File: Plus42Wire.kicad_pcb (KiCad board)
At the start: 2 copper layers, 60.8 x 99.9 mm, 32 parts, among them CN1 EDGE_CONN, CN2 CONN_I2C_1, CN3 CONN_I2C_1, CN4 CONN_I2C_1, U1 GAL20V8, U2 PCF8584, U3 24LC16, U4 DS1307+, Y1 12 MHz, Y2 32768 kHz

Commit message: Add 3.3V bus
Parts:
- removed R7: 47, Resistor_THT:R_Axial_DIN0207_L6.3mm_D2.5mm_P2.54mm_Vertical
- added C10: 10u, Capacitor_THT:CP_Radial_D6.3mm_P2.50mm, F.Cu at (135.3, 87.5)
- added C8: 100n, Capacitor_THT:C_Disc_D7.0mm_W2.5mm_P5.00mm, F.Cu at (125.1, 79.9)
- added C9: 100n, Capacitor_THT:C_Disc_D7.0mm_W2.5mm_P5.00mm, F.Cu at (135.3, 74.9)
- added CN5: CONN_I2C_3V3, Connector_PinHeader_2.54mm:PinHeader_1x04_P2.54mm_Vertical, F.Cu at (126.4, 68.5)
- added CN6: CONN_I2C_3V3, Connector_PinHeader_2.54mm:PinHeader_1x04_P2.54mm_Vertical, F.Cu at (148.3, 68.5)
- added CN7: CONN_I2C_3V3, Connector_PinHeader_2.54mm:PinHeader_1x04_P2.54mm_Vertical, F.Cu at (170.4, 68.5)
- added Q1: TN2106, Package_TO_SOT_THT:TO-92L_HandSolder, F.Cu at (139.6, 79.9)
- added Q2: TN2106, Package_TO_SOT_THT:TO-92L_HandSolder, F.Cu at (140.3, 76.2)
- added R4: 47, Resistor_THT:R_Axial_DIN0207_L6.3mm_D2.5mm_P10.16mm_Horizontal, F.Cu at (125.1, 92.6)
- added R5: 4.7k, Resistor_THT:R_Axial_DIN0207_L6.3mm_D2.5mm_P10.16mm_Horizontal, F.Cu at (148.7, 83.1)
- added R6: 4.7k, Resistor_THT:R_Axial_DIN0207_L6.3mm_D2.5mm_P10.16mm_Horizontal, F.Cu at (144.9, 83.1)
- added U5: MCP1700-3302E_TO92, Package_TO_SOT_THT:TO-92L_HandSolder, F.Cu at (130.2, 78.9)
- CN2: renamed from CN4; value CONN_I2C_1 -> CONN_I2C_5V
- CN3: renamed from CN2; value CONN_I2C_1 -> CONN_I2C_5V
- CN4: renamed from CN3; value CONN_I2C_1 -> CONN_I2C_5V
- moved Y2 14.2 mm to (141.1, 102.2)
- moved CN4 10.6 mm to (170.3, 52.8), turned to 90 degrees
- moved FB2 9.25 mm to (125.1, 87.5), turned to 0 degrees
- moved CN3 8.82 mm to (148.3, 52.8), turned to 90 degrees
- moved CN2 8.13 mm to (126.4, 52.8), turned to 90 degrees
- moved C3 6.39 mm to (144.9, 90.8), turned to 0 degrees
- moved BAT1 0.37 mm to (172.5, 81.2)
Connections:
- Y2 pad 1: Net-(U4-Pad2) -> Net-(U4-Pad1)
- Y2 pad 2: Net-(U4-Pad1) -> Net-(U4-Pad2)
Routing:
- net +3V3: track 0.00 -> 97.9 mm
- net /scl_3v3: track 0.00 -> 72.1 mm, vias 0 -> 1
- net /sda_3v3: track 0.00 -> 62.6 mm, vias 0 -> 1
- net +5V: track 243.0 -> 288.0 mm, vias 2 -> 3
- net /scl: track 161.1 -> 179.5 mm, vias 2 -> 3
- net /sda: track 168.7 -> 184.7 mm, vias 4 -> 5
- net Net-(U4-Pad1): track 13.8 -> 3.81 mm
- net Net-(FB2-Pad2): track 3.62 -> 8.26 mm
- net Net-(U4-Pad2): track 13.8 -> 10.4 mm
- net /clock: track 42.3 -> 45.5 mm
- net Net-(R4-Pad1): track 13.1 -> 13.6 mm
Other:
- board text added: "+3.3V"
- board text added: "+5V"
- board text added: "GND"
- board text added: "SCL"
- board text added: "SDA"

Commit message: Ready for V1rc1
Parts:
- C10: footprint Capacitor_THT:CP_Radial_D6.3mm_P2.50mm -> Capacitor_THT:CP_Radial_D5.0mm_P2.00mm
- CN4: value CONN_I2C_5V -> CONN_I2C_5V_ALT
- CN7: value CONN_I2C_3V3 -> CONN_I2C_3V3_ALT
- V1: footprint SoundX:logo -> Plus42Wire:Logo
- moved V1 1.82 mm to (146.1, 135.6)
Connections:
- CN4 pad 1: GND -> +5V
- CN4 pad 2: +5V -> GND
- CN4 pad 3: /sda -> /scl
- CN4 pad 4: /scl -> /sda
- CN7 pad 1: GND -> +3V3
- CN7 pad 2: +3V3 -> GND
- CN7 pad 3: /sda_3v3 -> /scl_3v3
- CN7 pad 4: /scl_3v3 -> /sda_3v3
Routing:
- net /scl: track 179.5 -> 175.1 mm
- net /scl_3v3: track 72.1 -> 67.7 mm
- net /sda: track 184.7 -> 187.2 mm
- net +3V3: track 97.9 -> 95.3 mm
- net /sda_3v3: track 62.6 -> 65.1 mm
- net Net-(BAT1-Pad1): track 23.5 -> 24.9 mm
- net +5V: track 288.0 -> 286.7 mm, vias 3 -> 2
- net /d1: track 31.0 -> 32.1 mm
- net /~rd8584: track 27.5 -> 28.0 mm
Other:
- board text added: "12 MHz"
- board text added: "3.3V BUS"
- board text added: "5V BUS"
- board text added: "CR2032"
- board text added: "DIFFERENT"
- board text added: "PINOUT"

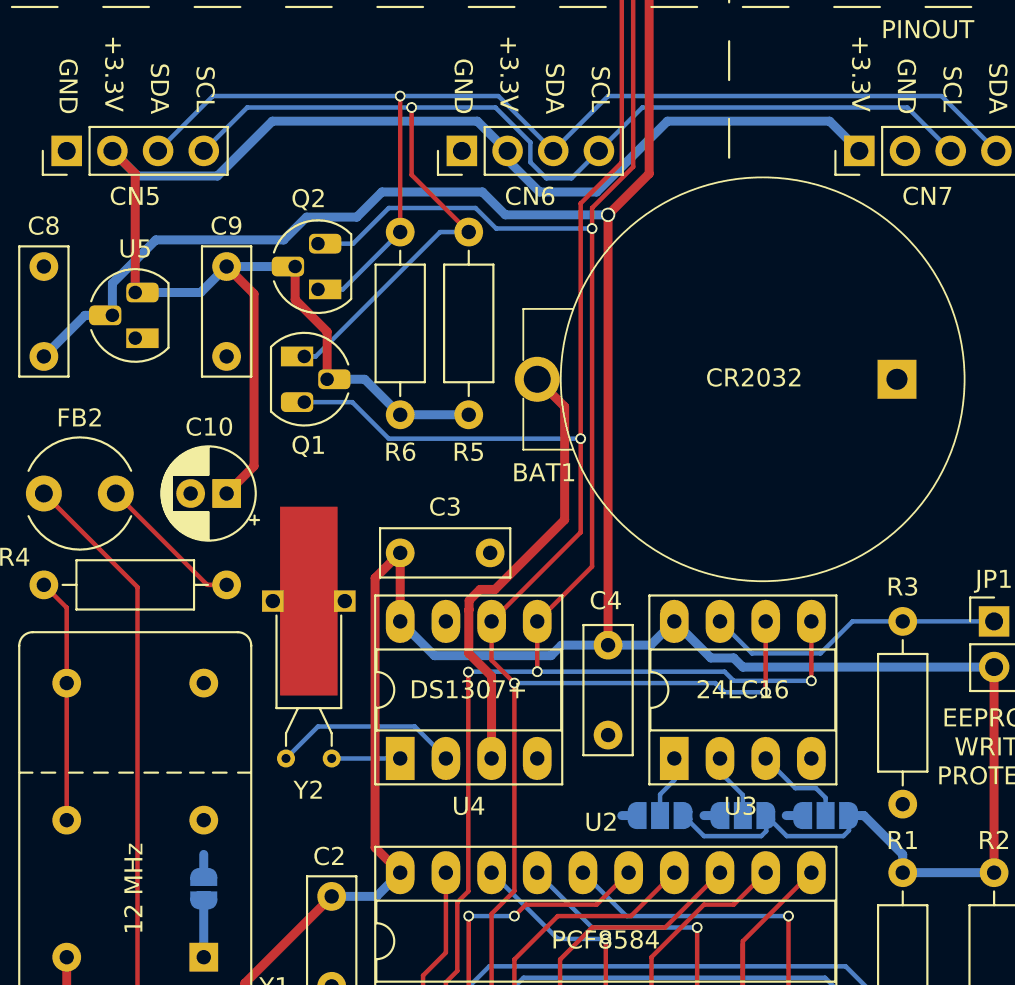
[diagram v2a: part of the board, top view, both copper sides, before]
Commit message: Add footprints for alternative MOSFETs
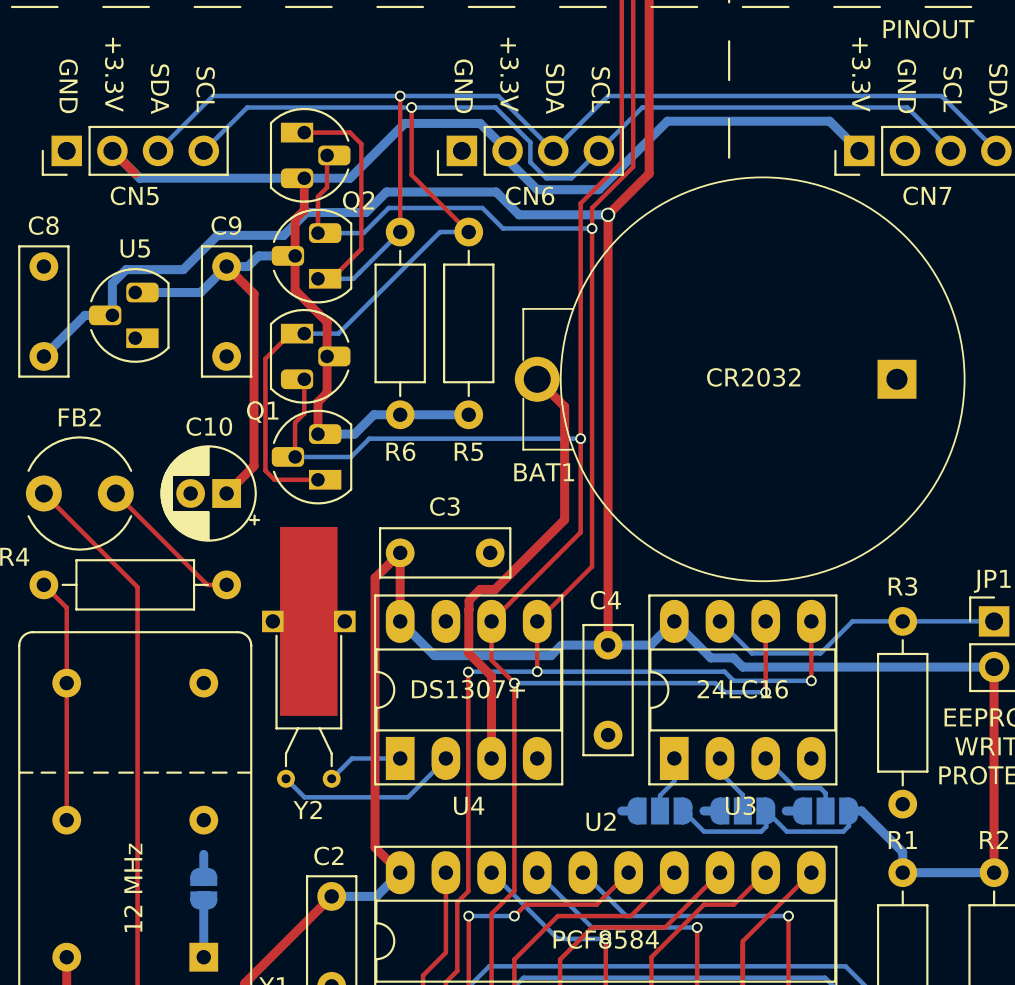
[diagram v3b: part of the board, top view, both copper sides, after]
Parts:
- added Q101: BSS88, Package_TO_SOT_THT:TO-92L_HandSolder, F.Cu at (140.3, 86.7)
- added Q102: BSS88, Package_TO_SOT_THT:TO-92L_HandSolder, F.Cu at (139.6, 67.4)
- moved Q1 1.27 mm to (139.6, 78.6)
- moved Y2 1.13 mm to (141.1, 103.4)
- moved Q2 0.59 mm to (140.3, 75.6)
- moved JP3 0.25 mm to (159.4, 105.2)
- moved JP4 0.25 mm to (164.0, 105.2)
- moved JP5 0.25 mm to (168.6, 105.2)
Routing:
- net /sda_3v3: track 65.1 -> 77.2 mm
- net /scl_3v3: track 67.7 -> 79.3 mm
- net /scl: track 175.1 -> 179.7 mm
- net /sda: track 187.2 -> 191.5 mm
- net +3V3: track 95.3 -> 97.4 mm
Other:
- board text added: "D"
- board text added: "G"
- board text added: "S"
